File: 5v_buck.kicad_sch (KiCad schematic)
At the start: 28 parts, among them U801 BUCK CONVERTER

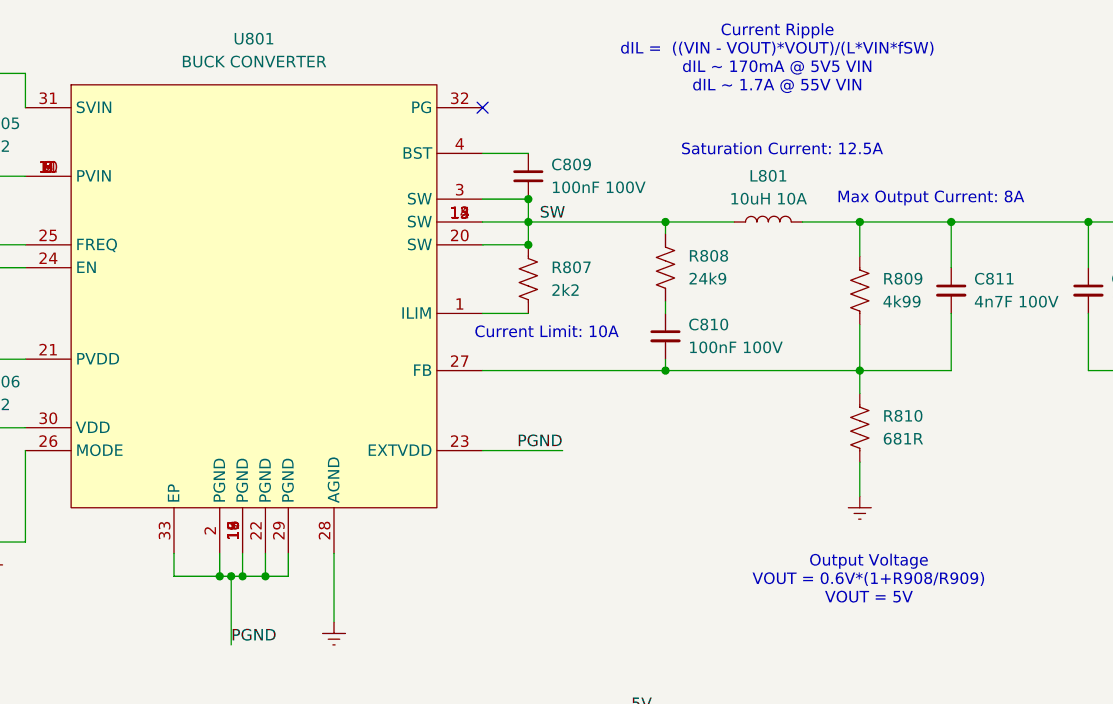
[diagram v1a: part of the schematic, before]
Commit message: switching dcdc
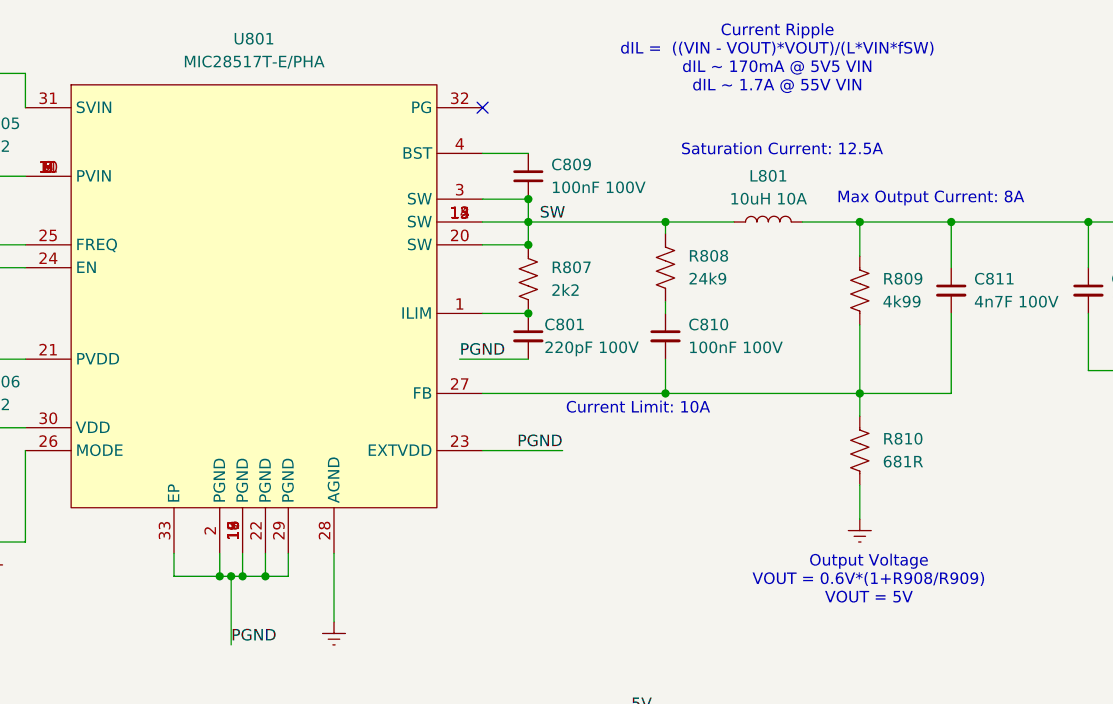
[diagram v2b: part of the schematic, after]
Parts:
- added C801: 220pF 100V, BR_Passives:C_0402_1005Metric-minimized, symbol BR_Capacitors_0402:C_0402_220pF_100V_C0G_5%
- U801: value BUCK CONVERTER -> MIC28517T-E/PHA
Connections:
- net PGND: now also C801.2
- net at R807.2, U801.1 (ILIM): now also C801.1
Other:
- moved on the sheet: R810

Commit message: more work
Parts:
- C811: footprint BR_Passives:C_0402_1005Metric -> BR_Passives:C_0402_1005Metric-minimized
- D801: value 5V -> LABEL
- NT801: value NetTie-2_0.18mm -> Net Tie
- TP801: value 5V -> TP_RING_TH
- TP802: value GND -> TP_RING_TH
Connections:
- net VOUT renamed 5V
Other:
- moved on the sheet: C806, R804, TP801, TP802

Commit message: more work
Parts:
- renumbered C803 to C801, C804 to C802, C805 to C803, C807 to C804, C806 to C805, C808 to C806, C809 to C807, C801 to C808, C810 to C809, C811 to C810, C812 to C811, C813 to C812, R804 to R803, R803 to R804, R811 to R809, R809 to R810, R810 to R811, TP802 to TP801, TP801 to TP802

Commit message: work
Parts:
- removed TP801, TP802: TP_RING_TH, BR_Connectors:TEST-TH_BD2.54-P1.4_RED, symbol BR_Connectors:TP_Ring_PTH
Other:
- moved on the sheet: C801, C802, C803, C804, C805, C806, C807, C808, C809, C810, C811, C812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

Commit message: missed a save
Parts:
- D801: value LABEL -> 5V
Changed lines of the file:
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@@
 			)
 		)
-		(property "Value" "LABEL"
+		(property "Value" "5V"
 			(at 309.88 251.5234 90)
 			(show_name no)

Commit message: fixing some errors
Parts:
- R802, R804: footprint BR_Passives:C_0402_1005Metric-minimized -> BR_Passives:R_0402_1005Metric-minimized
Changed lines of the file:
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@@
 			)
 		)
-		(property "Footprint" "BR_Passives:C_0402_1005Metric-minimized"
+		(property "Footprint" "BR_Passives:R_0402_1005Metric-minimized"
 			(at 218.44 102.87 0)
 			(hide yes)
@@
 			)
 		)
-		(property "Footprint" "BR_Passives:C_0402_1005Metric-minimized"
+		(property "Footprint" "BR_Passives:R_0402_1005Metric-minimized"
 			(at 198.12 123.19 0)
 			(hide yes)

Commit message: getting really close to final
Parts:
- R801, R803, R808, R809, R810, R811: footprint BR_Passives:C_0402_1005Metric-minimized -> BR_Passives:R_0402_1005Metric-minimized
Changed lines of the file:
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@@
 			)
 		)
-		(property "Footprint" "BR_Passives:C_0402_1005Metric-minimized"
+		(property "Footprint" "BR_Passives:R_0402_1005Metric-minimized"
 			(at 290.83 182.88 0)
 			(hide yes)
@@
 			)
 		)
-		(property "Footprint" "BR_Passives:C_0402_1005Metric-minimized"
+		(property "Footprint" "BR_Passives:R_0402_1005Metric-minimized"
 			(at 327.66 111.76 0)
 			(hide yes)
@@
 			)
 		)
-		(property "Footprint" "BR_Passives:C_0402_1005Metric-minimized"
+		(property "Footprint" "BR_Passives:R_0402_1005Metric-minimized"
 			(at 306.07 163.83 0)
 			(hide yes)
@@
 			)
 		)
-		(property "Footprint" "BR_Passives:C_0402_1005Metric-minimized"
+		(property "Footprint" "BR_Passives:R_0402_1005Metric-minimized"
 			(at 327.66 129.54 0)
 			(hide yes)
@@
 			)
 		)
-		(property "Footprint" "BR_Passives:C_0402_1005Metric-minimized"
+		(property "Footprint" "BR_Passives:R_0402_1005Metric-minimized"
 			(at 198.12 109.22 0)
 			(hide yes)
@@
 			)
 		)
-		(property "Footprint" "BR_Passives:C_0402_1005Metric-minimized"
+		(property "Footprint" "BR_Passives:R_0402_1005Metric-minimized"
 			(at 306.07 261.62 0)
 			(hide yes)
